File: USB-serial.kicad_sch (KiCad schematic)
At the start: 2 parts, among them IC1 USB-UART, J1 USB-C

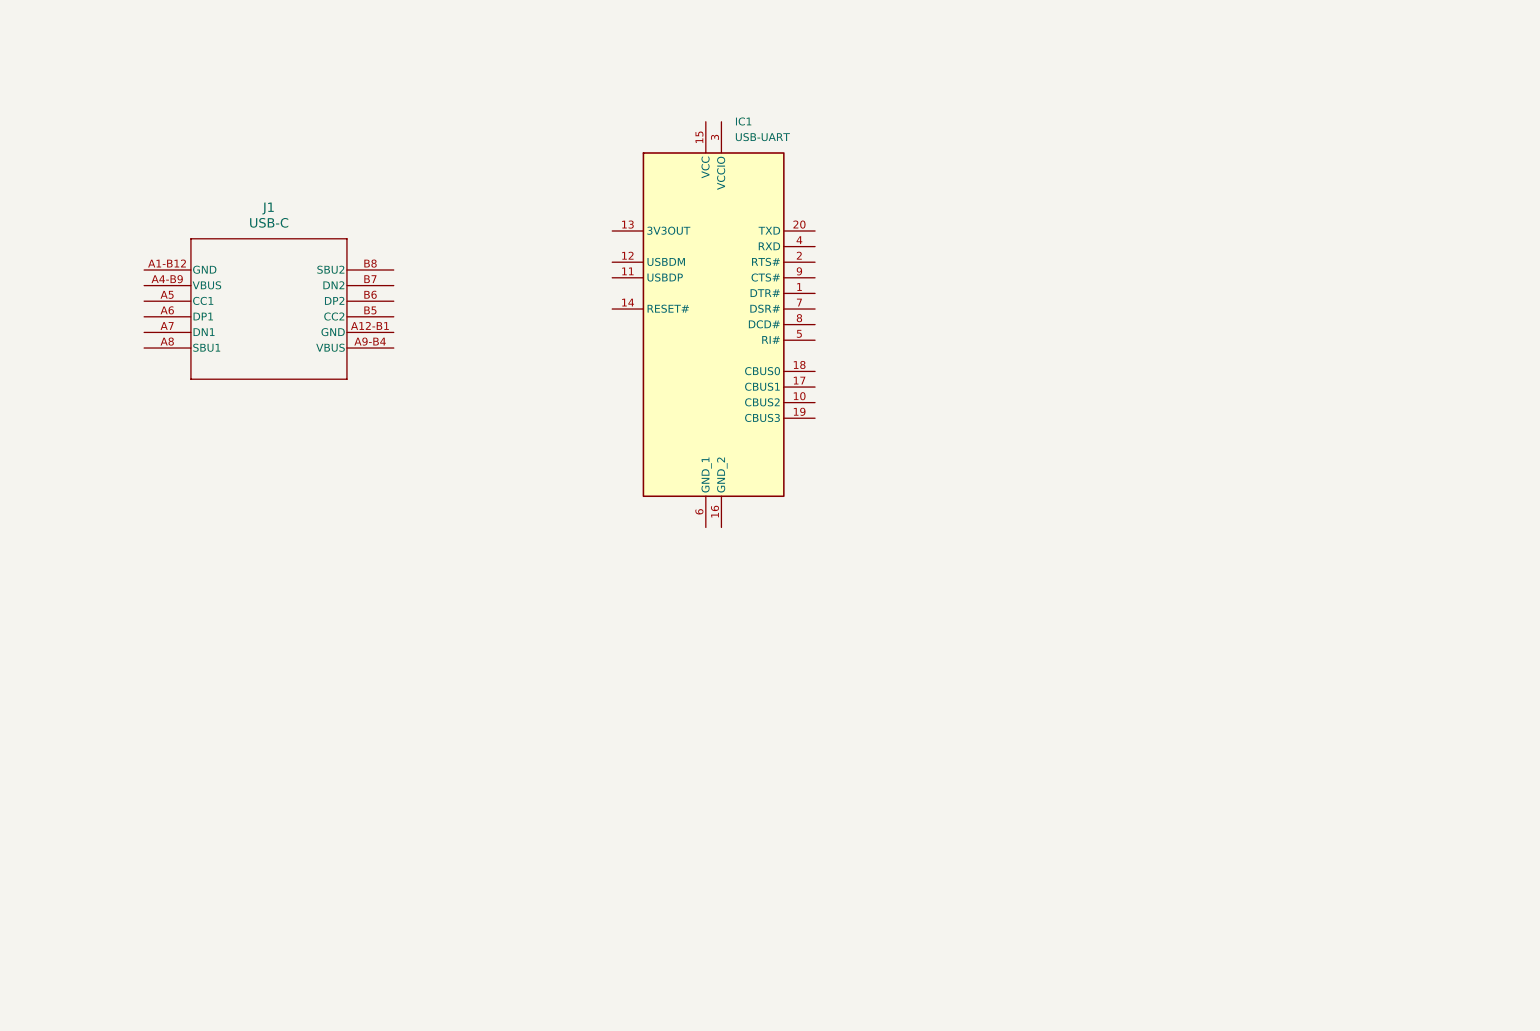
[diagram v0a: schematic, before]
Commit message: usb serial additions
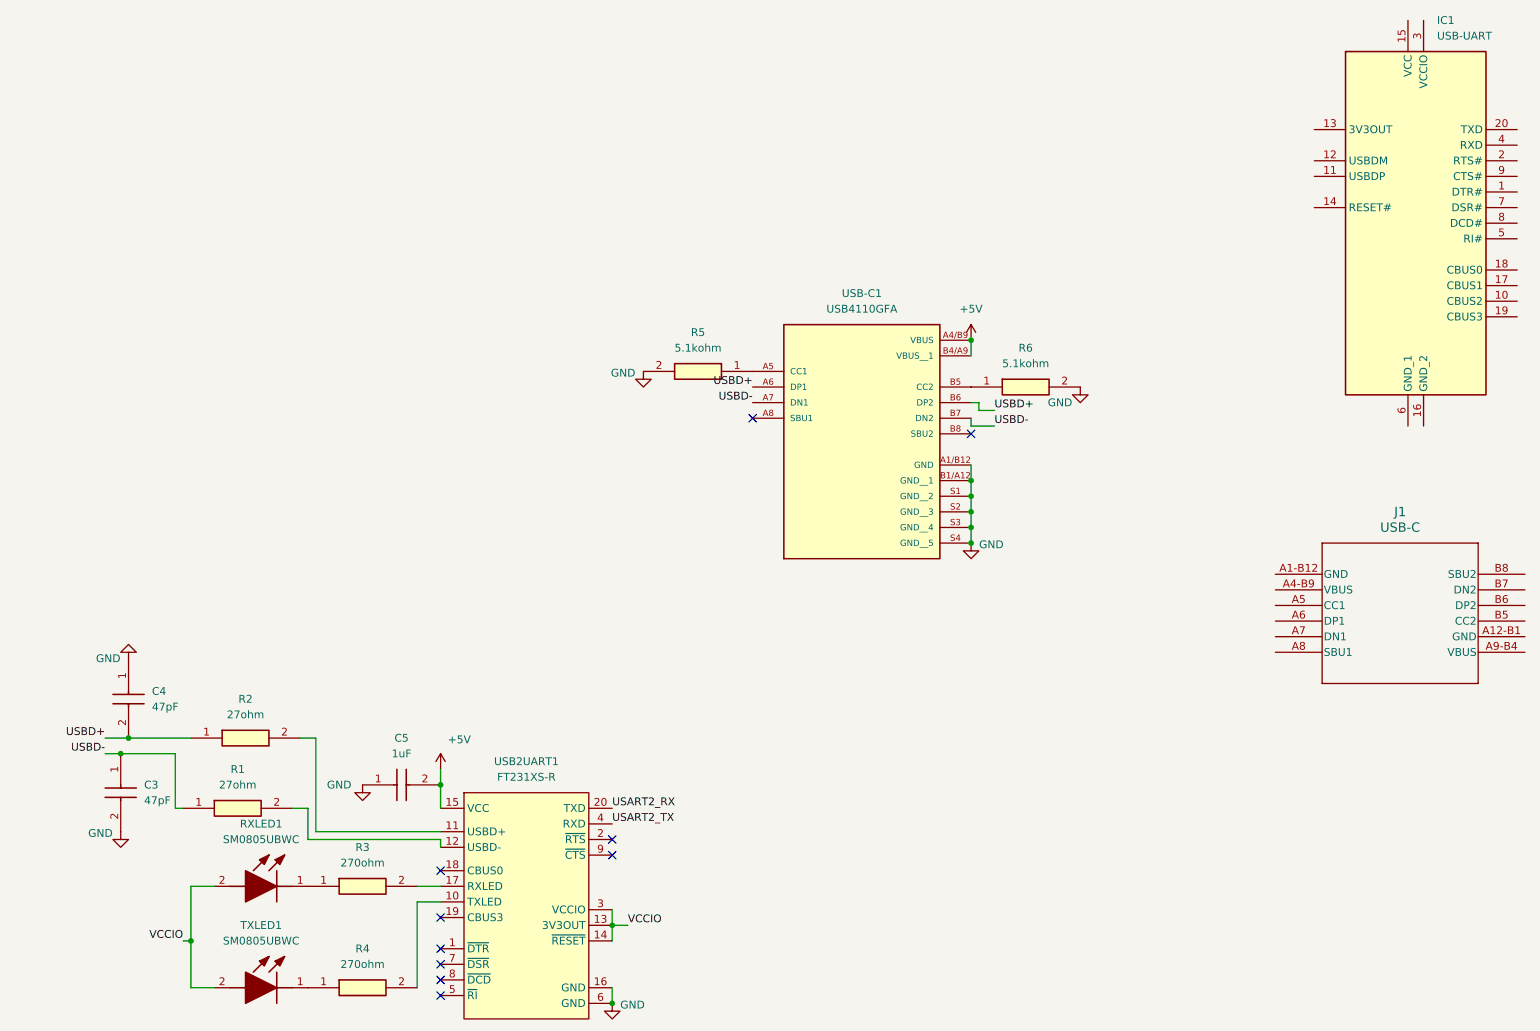
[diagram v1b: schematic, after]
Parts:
- added C3, C4: 47pF, Capacitor_SMD:C_0805_2012Metric, symbol 08055A470JAT2A:08055A470JAT2A
- added C5: 1uF, Capacitor_SMD:C_0805_2012Metric, symbol CC0805KRX5R6BB105:CC0805KRX5R6BB105
- added R1, R2: 27ohm, Resistor_SMD:R_0805_2012Metric, symbol CR0805-FX-27R0ELF:CR0805-FX-27R0ELF
- added R3, R4: 270ohm, Resistor_SMD:R_0805_2012Metric, symbol CR0805-FX-2700ELF:CR0805-FX-2700ELF
- added R5, R6: 5.1kohm, Resistor_SMD:R_0805_2012Metric, symbol CR0805-FX-27R0ELF:CR0805-FX-27R0ELF
- added RXLED1, TXLED1: SM0805UBWC, KiCad0805:LEDC2012X110N, symbol group127:SerialLED
- added USB-C1: USB4110GFA, USB4110_GF_A:GCT_USB4110GFA, symbol group127:USB-C-Port
- added USB2UART1: FT231XS-R, Package_SO:SSOP-20_3.9x8.7mm_P0.635mm, symbol group127:USB2UART
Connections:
- new net: R4.1, TXLED1.1 (K)
- new net: R4.2, USB2UART1.10 (TXLED)
- new net: R6.1, USB-C1.B5 (CC2)
- new net: R2.2, USB2UART1.11 (USBD+)
- new net: R1.2, USB2UART1.12 (USBD-)
- new net: R3.1, RXLED1.1 (K)
- new net: R3.2, USB2UART1.17 (RXLED)
- new net: R5.1, USB-C1.A5 (CC1)
- new net +5V: C5.2, USB-C1.A4/B9 (VBUS), USB-C1.B4/A9 (VBUS__1), USB2UART1.15 (VCC)
- new net GND: C3.2, C4.1, C5.1, R5.2, R6.2, USB-C1.A1/B12 (GND), USB-C1.B1/A12 (GND__1), USB-C1.S1 (GND__2), USB-C1.S2 (GND__3), USB-C1.S3 (GND__4), USB-C1.S4 (GND__5), USB2UART1.16 (GND), USB2UART1.6 (GND)
- new net USART2_RX: USB2UART1.20 (TXD)
- new net USART2_TX: USB2UART1.4 (RXD)
- new net USBD+: C4.2, R2.1, USB-C1.A6 (DP1), USB-C1.B6 (DP2)
- new net USBD-: C3.1, R1.1, USB-C1.A7 (DN1), USB-C1.B7 (DN2)
- new net VCCIO: RXLED1.2 (A), TXLED1.2 (A), USB2UART1.13 (3V3OUT), USB2UART1.14 (~{RESET}), USB2UART1.3 (VCCIO)
- no-connect marks 0 -> 10
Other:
- moved on the sheet: IC1, J1

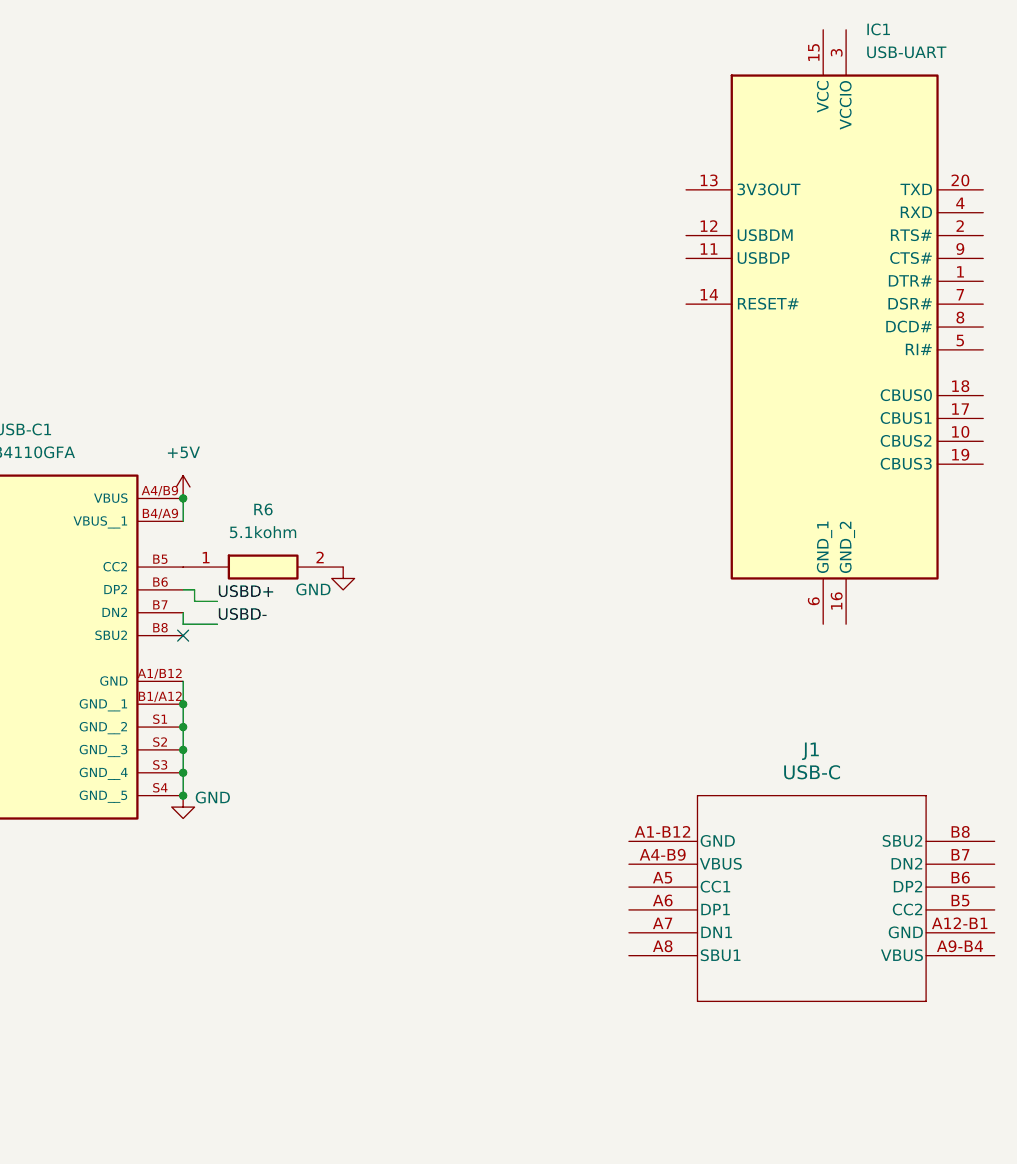
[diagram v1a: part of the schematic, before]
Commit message: merged Mike's USB-serial changes
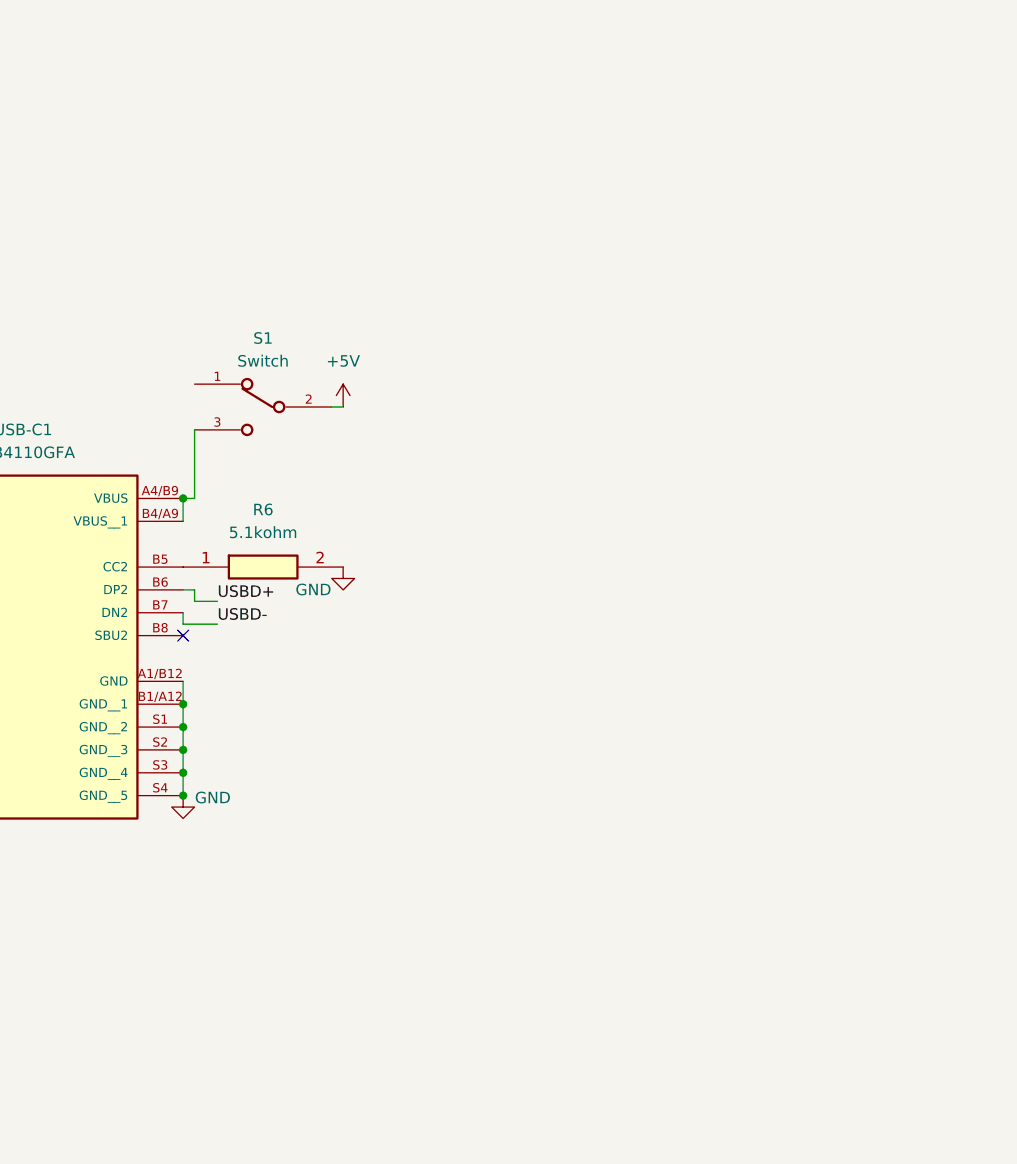
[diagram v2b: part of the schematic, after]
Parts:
- removed IC1: USB-UART, SOP64P599X175-20N, symbol group127:USB-UART
- removed J1: USB-C, USB4110-GF-A_GCT, symbol group127:USB-C
- added S1: Switch, JS102011SAQN:SW_JS102011SAQN, symbol Project1LibUniv:Switch
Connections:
- net +5V: now also S1.2; no longer USB-C1.A4/B9 (VBUS), USB-C1.B4/A9 (VBUS__1)
- new net: S1.3, USB-C1.A4/B9 (VBUS), USB-C1.B4/A9 (VBUS__1)
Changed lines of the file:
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@@
+	(wire
+		(pts
+			(xy 190.5 62.23) (xy 190.5 69.85)
+		)
+		(stroke
+			(width 0)
+			(type default)
+		)
+	)
 	(wire
 		(pts
@@
 	(wire
 		(pts
+			(xy 207.01 59.69) (xy 205.74 59.69)
+		)
+		(stroke
+			(width 0)
+			(type default)
+		)
+	)
+	(wire
+		(pts
 			(xy 130.81 162.56) (xy 130.81 165.1)
 		)
@@
 		(pts
 			(xy 130.81 165.1) (xy 130.81 167.64)
+		)
+		(stroke
+			(width 0)
+			(type default)
+		)
+	)
+	(wire
+		(pts
+			(xy 190.5 69.85) (xy 189.23 69.85)
 		)
 		(stroke
@@
 	)
 	(symbol
-		(lib_id "group127:USB-C")
-		(at 259.08 114.3 0)
+		(lib_id "Project1LibUniv:Switch")
+		(at 198.12 59.69 0)
 		(unit 1)
 		(exclude_from_sim no)
@@
 		(dnp no)
 		(fields_autoplaced yes)
-		(property "Reference" "J1"
-			(at 259.08 97.79 0)
-			(effects
-				(font
-					(size 1.524 1.524)
-				)
-			)
-		)
-		(property "Value" "USB-C"
-			(at 259.08 100.33 0)
-			(effects
-				(font
-					(size 1.524 1.524)
-				)
-			)
-		)
-		(property "Footprint" "USB4110-GF-A_GCT"
-			(at 259.08 119.126 0)
-			(effects
-				(font
-					(size 1.27 1.27)
-					(italic yes)
-				)
-				(hide yes)
-			)
-		)
-		(property "Datasheet" "USB4110-GF-A"
-			(at 258.572 109.982 0)
-			(effects
-				(font
-					(size 1.27 1.27)
-					(italic yes)
+		(property "Reference" "S1"
+			(at 198.12 52.07 0)
+			(effects
+				(font
+					(size 1.27 1.27)
+				)
+			)
+		)
+		(property "Value" "Switch"
+			(at 198.12 54.61 0)
+			(effects
+				(font
+					(size 1.27 1.27)
+				)
+			)
+		)
+		(property "Footprint" "JS102011SAQN:SW_JS102011SAQN"
+			(at 198.12 59.69 0)
+			(effects
+				(font
+					(size 1.27 1.27)
+				)
+				(justify bottom)
+				(hide yes)
+			)
+		)
+		(property "Datasheet" ""
+			(at 198.12 59.69 0)
+			(effects
+				(font
+					(size 1.27 1.27)
 				)
 				(hide yes)
@@
 		)
 		(property "Description" ""
-			(at 238.76 107.95 0)
-			(effects
-				(font
-					(size 1.27 1.27)
-				)
-				(hide yes)
-			)
-		)
-		(pin "A4-B9"
-		)
-		(pin "A6"
-		)
-		(pin "B8"
-		)
-		(pin "A8"
-		)
-		(pin "A1-B12"
-		)
-		(pin "B6"
-		)
-		(pin "A7"
-		)
-		(pin "B7"
-		)
-		(pin "A12-B1"
-		)
-		(pin "A9-B4"
-		)
-		(pin "A5"
-		)
-		(pin "B5"
+			(at 198.12 59.69 0)
+			(effects
+				(font
+					(size 1.27 1.27)
+				)
+				(hide yes)
+			)
+		)
+		(property "MANUFACTURER" "C&K"
+			(at 198.12 59.69 0)
+			(effects
+				(font
+					(size 1.27 1.27)
+				)
+				(justify bottom)
+				(hide yes)
+			)
+		)
+		(pin "1"
+		)
+		(pin "2"
+		)
+		(pin "3"
 		)
 		(instances
 			(project ""
 				(path "/5ce3566e-4e0f-420e-9b0d-3952cd3c63fd/8f41fec2-6210-43dd-9328-85befbc13075"
-					(reference "J1")
+					(reference "S1")
 					(unit 1)
 				)
@@
 	(symbol
 		(lib_id "power:+5V")
-		(at 189.23 69.85 0)
+		(at 207.01 59.69 0)
 		(mirror y)
 		(unit 1)
@@
 		(dnp no)
 		(property "Reference" "#PWR012"
-			(at 189.23 73.66 0)
+			(at 207.01 63.5 0)
 			(effects
 				(font
@@
 		)
 		(property "Value" "+5V"
-			(at 189.23 64.77 0)
+			(at 207.01 54.61 0)
 			(effects
 				(font
@@
 		)
 		(property "Footprint" ""
-			(at 189.23 69.85 0)
+			(at 207.01 59.69 0)
 			(effects
 				(font
@@
 		)
 		(property "Datasheet" ""
-			(at 189.23 69.85 0)
+			(at 207.01 59.69 0)
 			(effects
 				(font
@@
 		)
 		(property "Description" "Power symbol creates a global label with name \"+5V\""
-			(at 189.23 69.85 0)
+			(at 207.01 59.69 0)
 			(effects
 				(font
@@
 					(unit 1)
 				)
-			)
-		)
-	)
-	(symbol
-		(lib_id "group127:USB-UART")
-		(at 259.08 39.37 0)
-		(unit 1)
-		(exclude_from_sim no)
-		(in_bom yes)
-		(on_board yes)
-		(dnp no)
-		(fields_autoplaced yes)
-		(property "Reference" "IC1"
-			(at 265.0841 17.78 0)
-			(effects
-				(font
-					(size 1.27 1.27)
-				)
-				(justify left)
-			)
-		)
-		(property "Value" "USB-UART"
-			(at 265.0841 20.32 0)
-			(effects
-				(font
-					(size 1.27 1.27)
-				)
-				(justify left)
-			)
-		)
-		(property "Footprint" "SOP64P599X175-20N"
-			(at 288.29 124.13 0)
-			(effects
-				(font
-					(size 1.27 1.27)
-				)
-				(justify left top)
-				(hide yes)
-			)
-		)
-		(property "Datasheet" "https://datasheet.datasheetarchive.com/originals/distributors/Datasheets_SAMA/824938d1687833d6997706543241551a.pdf"
-			(at 288.29 224.13 0)
-			(effects
-				(font
-					(size 1.27 1.27)
-				)
-				(justify left top)
-				(hide yes)
-			)
-		)
-		(property "Description" "FTDI Chip FT231XS-R, Interface RS232, RS422, RS485, SIE, UART 3MBd, 5 V, 20-pin, SSOP"
-			(at 269.748 88.646 0)
-			(effects
-				(font
-					(size 1.27 1.27)
-				)
-				(hide yes)
-			)
-		)
-		(property "Height" "1.753"
-			(at 288.29 424.13 0)
-			(effects
-				(font
-					(size 1.27 1.27)
-				)
-				(justify left top)
-				(hide yes)
-			)
-		)
-		(property "Mouser Part Number" "895-FT231XS-R"
-			(at 288.29 524.13 0)
-			(effects
-				(font
-					(size 1.27 1.27)
-				)
-				(justify left top)
-				(hide yes)
-			)
-		)
-		(property "Mouser Price/Stock" "https://www.mouser.co.uk/ProductDetail/FTDI/FT231XS-R?qs=Gp1Yz1mis3WduRPsgrTbtg%3D%3D"
-			(at 288.29 624.13 0)
-			(effects
-				(font
-					(size 1.27 1.27)
-				)
-				(justify left top)
-				(hide yes)
-			)
-		)
-		(property "Manufacturer_Name" "FTDI Chip"
-			(at 288.29 724.13 0)
-			(effects
-				(font
-					(size 1.27 1.27)
-				)
-				(justify left top)
-				(hide yes)
-			)
-		)
-		(property "Manufacturer_Part_Number" "FT231XS-R"
-			(at 288.29 824.13 0)
-			(effects
-				(font
-					(size 1.27 1.27)
-				)
-				(justify left top)
-				(hide yes)
-			)
-		)
-		(pin "16"
-		)
-		(pin "19"
-		)
-		(pin "1"
-		)
-		(pin "10"
-		)
-		(pin "11"
-		)
-		(pin "12"
-		)
-		(pin "13"
-		)
-		(pin "14"
-		)
-		(pin "15"
-		)
-		(pin "17"
-		)
-		(pin "18"
-		)
-		(pin "2"
-		)
-		(pin "20"
-		)
-		(pin "3"
-		)
-		(pin "4"
-		)
-		(pin "5"
-		)
-		(pin "6"
-		)
-		(pin "8"
-		)
-		(pin "9"
-		)
-		(pin "7"
-		)
-		(instances
-			(project ""
-				(path "/5ce3566e-4e0f-420e-9b0d-3952cd3c63fd/8f41fec2-6210-43dd-9328-85befbc13075"
-					(reference "IC1")
-					(unit 1)
-				)
